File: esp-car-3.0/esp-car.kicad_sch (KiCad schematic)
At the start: 36 parts, among them J1 Conn_01x07_Socket, J2 Conn_01x07_Socket, U1 ESP32-DEVKIT-V1, U3 L293D

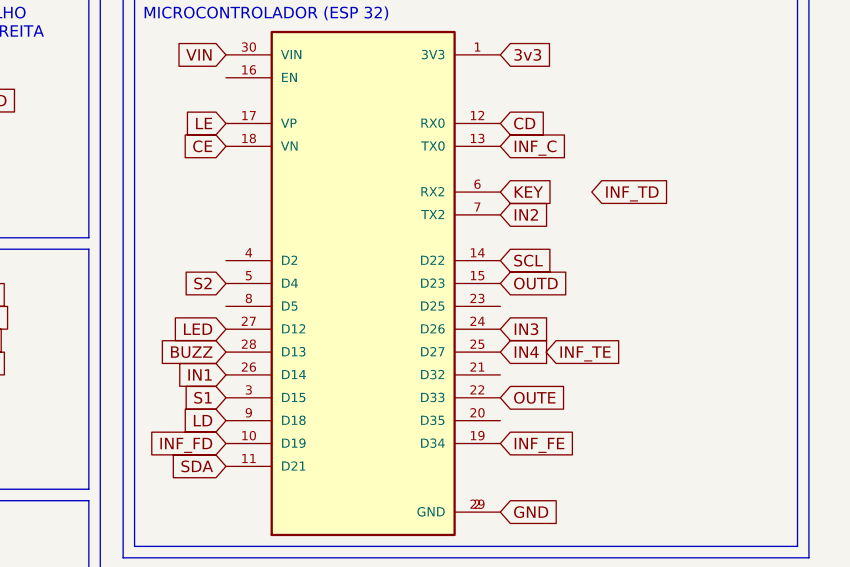
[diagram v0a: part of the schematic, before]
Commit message: finalizado, tem que revisar, esp_car_3.3
revisa os pinos e muda, trabalhe com o stevan vitor
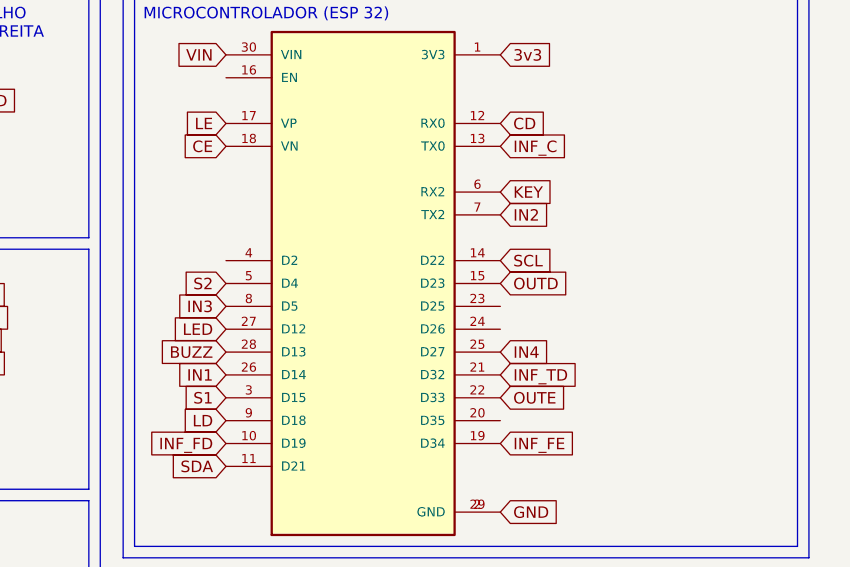
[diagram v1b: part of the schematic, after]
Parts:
- ALI1, MotorD1, MotorE1: footprint IFSUL Camaquã:TerminalBlock_Phoenix_MKDS-1,5-2-5.08_1x02_P5.08mm_Horizontal -> Connector_PinSocket_2.54mm:PinSocket_1x02_P2.54mm_Vertical
- H3, H4: footprint (none) -> MountingHole:MountingHole_3.2mm_M3
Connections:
- net IN3: now also U1.8 (D5); no longer U1.24 (D26)
- net INF_TD: now also U1.21 (D32)
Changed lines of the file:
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@@
 	(global_label "IN3"
 		(shape input)
-		(at 127 54.61 0)
+		(at 96.52 52.07 180)
 		(fields_autoplaced yes)
 		(effects
@@
 				(size 1.27 1.27)
 			)
-			(justify left)
+			(justify right)
 		)
 		(property "Intersheetrefs" "${INTERSHEET_REFS}"
-			(at 133.13 54.61 0)
+			(at 90.39 52.07 0)
 			(effects
 				(font
 					(size 1.27 1.27)
 				)
-				(justify left)
+				(justify right)
 				(hide yes)
 			)
@@
 		)
 	)
-	(global_label "INF_TE"
-		(shape input)
-		(at 132.08 57.15 0)
-		(fields_autoplaced yes)
-		(effects
-			(font
-				(size 1.27 1.27)
-			)
-			(justify left)
-		)
-		(property "Intersheetrefs" "${INTERSHEET_REFS}"
-			(at 141.1733 57.15 0)
-			(effects
-				(font
-					(size 1.27 1.27)
-				)
-				(justify left)
-				(hide yes)
-			)
-		)
-	)
 	(global_label "SDA"
 		(shape input)
@@
 	(global_label "INF_TD"
 		(shape input)
-		(at 137.16 39.37 0)
+		(at 127 59.69 0)
 		(fields_autoplaced yes)
 		(effects
@@
 		)
 		(property "Intersheetrefs" "${INTERSHEET_REFS}"
-			(at 146.3743 39.37 0)
+			(at 136.2143 59.69 0)
 			(effects
 				(font
@@
 			)
 		)
-		(property "Footprint" ""
+		(property "Footprint" "MountingHole:MountingHole_3.2mm_M3"
 			(at 93.98 180.34 0)
 			(effects
@@
 			)
 		)
-		(property "Footprint" ""
+		(property "Footprint" "MountingHole:MountingHole_3.2mm_M3"
 			(at 105.41 180.34 0)
 			(effects
@@
 			)
 		)
-		(property "Footprint" "IFSUL Camaquã:TerminalBlock_Phoenix_MKDS-1,5-2-5.08_1x02_P5.08mm_Horizontal"
+		(property "Footprint" "Connector_PinSocket_2.54mm:PinSocket_1x02_P2.54mm_Vertical"
 			(at 134.62 93.98 0)
 			(effects
@@
 			)
 		)
-		(property "Footprint" "IFSUL Camaquã:TerminalBlock_Phoenix_MKDS-1,5-2-5.08_1x02_P5.08mm_Horizontal"
+		(property "Footprint" "Connector_PinSocket_2.54mm:PinSocket_1x02_P2.54mm_Vertical"
 			(at 134.62 105.41 0)
 			(effects
@@
 			)
 		)
-		(property "Footprint" "IFSUL Camaquã:TerminalBlock_Phoenix_MKDS-1,5-2-5.08_1x02_P5.08mm_Horizontal"
+		(property "Footprint" "Connector_PinSocket_2.54mm:PinSocket_1x02_P2.54mm_Vertical"
 			(at 158.75 184.15 0)
 			(effects

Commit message: finalizada agora
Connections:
- net CE: now also U1.23 (D25); no longer U1.18 (VN)
- net LE: now also U1.20 (D35); no longer U1.17 (VP)
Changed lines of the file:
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@@
 	(global_label "LE"
 		(shape input)
-		(at 96.52 31.75 180)
-		(fields_autoplaced yes)
-		(effects
-			(font
-				(size 1.27 1.27)
-			)
-			(justify right)
-		)
-		(property "Intersheetrefs" "${INTERSHEET_REFS}"
-			(at 91.3577 31.75 0)
-			(effects
-				(font
-					(size 1.27 1.27)
-				)
-				(justify right)
+		(at 127 64.77 0)
+		(fields_autoplaced yes)
+		(effects
+			(font
+				(size 1.27 1.27)
+			)
+			(justify left)
+		)
+		(property "Intersheetrefs" "${INTERSHEET_REFS}"
+			(at 132.1623 64.77 0)
+			(effects
+				(font
+					(size 1.27 1.27)
+				)
+				(justify left)
 				(hide yes)
 			)
@@
 	(global_label "CE"
 		(shape input)
-		(at 96.52 34.29 180)
-		(fields_autoplaced yes)
-		(effects
-			(font
-				(size 1.27 1.27)
-			)
-			(justify right)
-		)
-		(property "Intersheetrefs" "${INTERSHEET_REFS}"
-			(at 91.1158 34.29 0)
-			(effects
-				(font
-					(size 1.27 1.27)
-				)
-				(justify right)
-				(hide yes)
-			)
+		(at 127 52.07 0)
+		(fields_autoplaced yes)
+		(effects
+			(font
+				(size 1.27 1.27)
+			)
+			(justify left)
+		)
+		(property "Intersheetrefs" "${INTERSHEET_REFS}"
+			(at 132.4042 52.07 0)
+			(effects
+				(font
+					(size 1.27 1.27)
+				)
+				(justify left)
+				(hide yes)
+			)

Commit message: versão finalizada e polida
muitas alterações
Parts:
- added C2: C, Capacitor_THT:CP_Radial_D10.0mm_P3.50mm, symbol Device:C
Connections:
- net GND: now also C2.2
- net VIN: now also C2.1
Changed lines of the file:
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@@
+		)
+	)
+	(global_label "GND"
+		(shape input)
+		(at 184.15 135.89 270)
+		(fields_autoplaced yes)
+		(effects
+			(font
+				(size 1.27 1.27)
+			)
+			(justify right)
+		)
+		(property "Intersheetrefs" "${INTERSHEET_REFS}"
+			(at 184.15 142.7457 90)
+			(effects
+				(font
+					(size 1.27 1.27)
+				)
+				(justify right)
+				(hide yes)
+			)
 		)
 	)
@@
 		(property "Intersheetrefs" "${INTERSHEET_REFS}"
 			(at 131.1342 175.26 0)
+			(effects
+				(font
+					(size 1.27 1.27)
+				)
+				(justify left)
+				(hide yes)
+			)
+		)
+	)
+	(global_label "VIN"
+		(shape input)
+		(at 184.15 128.27 90)
+		(fields_autoplaced yes)
+		(effects
+			(font
+				(size 1.27 1.27)
+			)
+			(justify left)
+		)
+		(property "Intersheetrefs" "${INTERSHEET_REFS}"
+			(at 184.15 122.2609 90)
 			(effects
 				(font
@@
 					(unit 1)
 				)
+			)
+		)
+	)
+	(symbol
+		(lib_id "Device:C")
+		(at 184.15 132.08 0)
+		(unit 1)
+		(exclude_from_sim no)
+		(in_bom yes)
+		(on_board yes)
+		(dnp no)
+		(fields_autoplaced yes)
+		(property "Reference" "C2"
+			(at 187.96 130.8099 0)
+			(effects
+				(font
+					(size 1.27 1.27)
+				)
+				(justify left)
+			)
+		)
+		(property "Value" "C"
+			(at 187.96 133.3499 0)
+			(effects
+				(font
+					(size 1.27 1.27)
+				)
+				(justify left)
+			)
+		)
+		(property "Footprint" "Capacitor_THT:CP_Radial_D10.0mm_P3.50mm"
+			(at 185.1152 135.89 0)
+			(effects
+				(font
+					(size 1.27 1.27)
+				)
+				(hide yes)
+			)
+		)
+		(property "Datasheet" "~"
+			(at 184.15 132.08 0)
+			(effects
+				(font
+					(size 1.27 1.27)
+				)
+				(hide yes)
+			)
+		)
+		(property "Description" "Unpolarized capacitor"
+			(at 184.15 132.08 0)
+			(effects
+				(font
+					(size 1.27 1.27)
+				)
+				(hide yes)
+			)
+		)
+		(pin "1"
+		)
+		(pin "2"
+		)
+		(instances
+			(project "esp-car"
+				(path "/d21b542b-1246-4c6e-b3e1-1cc2382a01d2"
+					(reference "C2")
+					(unit 1)
+				)

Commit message: .
.
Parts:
- added extra2: Conn_01x01_Socket, Connector_PinSocket_2.54mm:PinSocket_1x01_P2.54mm_Vertical, symbol Connector:Conn_01x01_Socket
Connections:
- net 3v3: no longer J1.5 (Pin_5), J2.5 (Pin_5)
- net LE: now also U1.18 (VN); no longer U1.20 (D35)
- net C2: now reaches U1.24 (D26)
- net C2: now also J2.5 (Pin_5)
- net 2: now reaches U1.4 (D2)
- net 2: now also extra2.1 (Pin_1)
- new net C1: J1.5 (Pin_5), U1.20 (D35)
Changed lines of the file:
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@@
 		)
 	)
-	(global_label "VCC"
-		(shape input)
-		(at 38.1 86.36 0)
-		(fields_autoplaced yes)
-		(effects
-			(font
-				(size 1.27 1.27)
-			)
-			(justify left)
-		)
-		(property "Intersheetrefs" "${INTERSHEET_REFS}"
-			(at 44.7138 86.36 0)
-			(effects
-				(font
-					(size 1.27 1.27)
-				)
-				(justify left)
-				(hide yes)
-			)
-		)
-	)
 	(global_label "GND"
 		(shape input)
@@
 		)
 	)
+	(global_label "C2"
+		(shape input)
+		(at 21.59 86.36 0)
+		(fields_autoplaced yes)
+		(effects
+			(font
+				(size 1.27 1.27)
+			)
+			(justify left)
+		)
+		(property "Intersheetrefs" "${INTERSHEET_REFS}"
+			(at 27.0547 86.36 0)
+			(effects
+				(font
+					(size 1.27 1.27)
+				)
+				(justify left)
+				(hide yes)
+			)
+		)
+	)
 	(global_label "GND"
 		(shape input)
@@
 	(global_label "LE"
 		(shape input)
-		(at 127 64.77 0)
+		(at 96.52 34.29 180)
 		(fields_autoplaced yes)
 		(effects
@@
 				(size 1.27 1.27)
 			)
-			(justify left)
+			(justify right)
 		)
 		(property "Intersheetrefs" "${INTERSHEET_REFS}"
-			(at 132.1623 64.77 0)
+			(at 91.3577 34.29 0)
 			(effects
 				(font
 					(size 1.27 1.27)
 				)
-				(justify left)
+				(justify right)
 				(hide yes)
 			)
@@
 		)
 	)
+	(global_label "C1"
+		(shape input)
+		(at 127 64.77 0)
+		(fields_autoplaced yes)
+		(effects
+			(font
+				(size 1.27 1.27)
+			)
+			(justify left)
+		)
+		(property "Intersheetrefs" "${INTERSHEET_REFS}"
+			(at 132.4647 64.77 0)
+			(effects
+				(font
+					(size 1.27 1.27)
+				)
+				(justify left)
+				(hide yes)
+			)
+		)
+	)
 	(global_label "S1"
 		(shape input)
@@
 		)
 	)
+	(global_label "2"
+		(shape input)
+		(at 96.52 46.99 180)
+		(fields_autoplaced yes)
+		(effects
+			(font
+				(size 1.27 1.27)
+			)
+			(justify right)
+		)
+		(property "Intersheetrefs" "${INTERSHEET_REFS}"
+			(at 92.3253 46.99 0)
+			(effects
+				(font
+					(size 1.27 1.27)
+				)
+				(justify right)
+				(hide yes)
+			)
+		)
+	)
 	(global_label "SDA"
 		(shape input)
@@
 		)
 	)
+	(global_label "C1"
+		(shape input)
+		(at 38.1 86.36 0)
+		(fields_autoplaced yes)
+		(effects
+			(font
+				(size 1.27 1.27)
+			)
+			(justify left)
+		)
+		(property "Intersheetrefs" "${INTERSHEET_REFS}"
+			(at 43.5647 86.36 0)
+			(effects
+				(font
+					(size 1.27 1.27)
+				)
+				(justify left)
+				(hide yes)
+			)
+		)
+	)
 	(global_label "OUT2"
 		(shape input)
@@
 		)
 	)
+	(global_label "2"
+		(shape input)
+		(at 170.18 153.67 180)
+		(fields_autoplaced yes)
+		(effects
+			(font
+				(size 1.27 1.27)
+			)
+			(justify right)
+		)
+		(property "Intersheetrefs" "${INTERSHEET_REFS}"
+			(at 165.9853 153.67 0)
+			(effects
+				(font
+					(size 1.27 1.27)
+				)
+				(justify right)
+				(hide yes)
+			)
+		)
+	)
 	(global_label "GND"
 		(shape input)
@@
 		)
 	)
-	(global_label "VCC"
-		(shape input)
-		(at 21.59 86.36 0)
-		(fields_autoplaced yes)
-		(effects
-			(font
-				(size 1.27 1.27)
-			)
-			(justify left)
-		)
-		(property "Intersheetrefs" "${INTERSHEET_REFS}"
-			(at 28.2038 86.36 0)
-			(effects
-				(font
-					(size 1.27 1.27)
-				)
-				(justify left)
-				(hide yes)
-			)
-		)
-	)
 	(global_label "GND"
 		(shape input)
@@
 		)
 	)
+	(global_label "C2"
+		(shape input)
+		(at 127 54.61 0)
+		(fields_autoplaced yes)
+		(effects
+			(font
+				(size 1.27 1.27)
+			)
+			(justify left)
+		)
+		(property "Intersheetrefs" "${INTERSHEET_REFS}"
+			(at 132.4647 54.61 0)
+			(effects
+				(font
+					(size 1.27 1.27)
+				)
+				(justify left)
+				(hide yes)
+			)
+		)
+	)
 	(global_label "OUTE"
 		(shape input)
@@
 					(unit 1)
 				)
+			)
+		)
+	)
+	(symbol
+		(lib_id "Connector:Conn_01x01_Socket")
+		(at 175.26 153.67 0)
+		(unit 1)
+		(exclude_from_sim no)
+		(in_bom yes)
+		(on_board yes)
+		(dnp no)
+		(fields_autoplaced yes)
+		(property "Reference" "extra2"
+			(at 176.53 153.6699 0)
+			(effects
+				(font
+					(size 1.27 1.27)
+				)
+				(justify left)
+			)
+		)
+		(property "Value" "Conn_01x01_Socket"
+			(at 176.53 154.9399 0)
+			(effects
+				(font
+					(size 1.27 1.27)
+				)
+				(justify left)
+				(hide yes)
+			)
+		)
+		(property "Footprint" "Connector_PinSocket_2.54mm:PinSocket_1x01_P2.54mm_Vertical"
+			(at 175.26 153.67 0)
+			(effects
+				(font
+					(size 1.27 1.27)
+				)
+				(hide yes)
+			)
+		)
+		(property "Datasheet" "~"
+			(at 175.26 153.67 0)
+			(effects
+				(font
+					(size 1.27 1.27)
+				)
+				(hide yes)
+			)
+		)
+		(property "Description" "Generic connector, single row, 01x01, script generated"
+			(at 175.26 153.67 0)
+			(effects
+				(font
+					(size 1.27 1.27)
+				)
+				(hide yes)
+			)
+		)
+		(pin "1"
+		)
+		(instances
+			(project "esp-car"
+				(path "/d21b542b-1246-4c6e-b3e1-1cc2382a01d2"
+					(reference "extra2")
+					(unit 1)
+				)

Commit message: espcar newvember
modelo quadradao
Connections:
- net C1: now also U1.12 (RX0); no longer U1.20 (D35)
- net C2: now also U1.23 (D25); no longer U1.24 (D26)
- net CD: now also U1.20 (D35); no longer U1.12 (RX0)
- net CE: now also U1.24 (D26); no longer U1.23 (D25)
- net INF_FE: now also U1.22 (D33); no longer U1.19 (D34)
- net OUTE: now also U1.19 (D34); no longer U1.22 (D33)
